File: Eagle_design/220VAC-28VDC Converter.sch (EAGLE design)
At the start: 6 parts, among them J1 1X2-3.5MM, J2 1X2-3.5MM

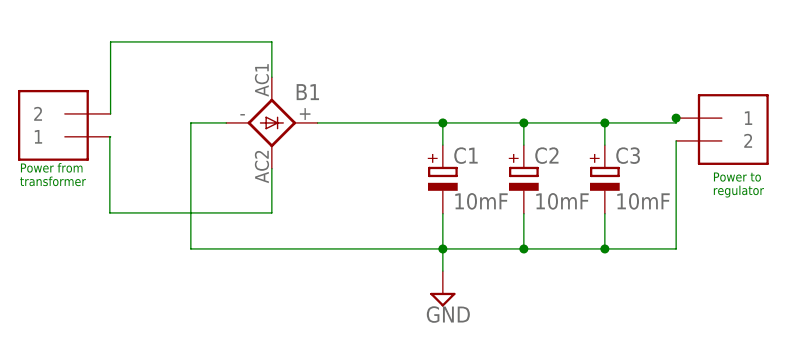
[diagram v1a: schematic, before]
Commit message: Adds labels to the wire connections
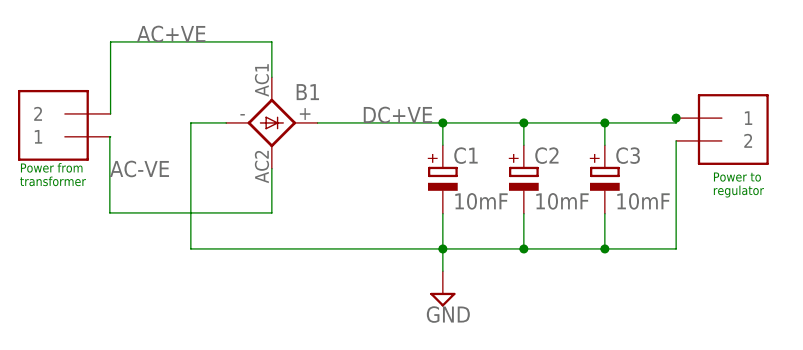
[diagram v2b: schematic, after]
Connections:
- net N$1 renamed AC+VE
- net N$2 renamed AC-VE
- net N$4 renamed DC+VE
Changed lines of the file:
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@@
 <setting verticaltext="up"/>
 </settings>
-<grid distance="0.1" unitdist="inch" unit="inch" style="lines" multiple="1" display="no" altdistance="0.01" altunitdist="inch" altunit="inch"/>
+<grid distance="1" unitdist="mm" unit="mm" style="lines" multiple="1" display="no" altdistance="1" altunitdist="mm" altunit="mm"/>
 <layers>
 <layer number="1" name="Top" color="4" fill="1" visible="no" active="no"/>
@@
 </busses>
 <nets>
-<net name="N$1" class="0">
+<net name="AC+VE" class="0">
 <segment>
 <pinref part="J1" gate="G$1" pin="2"/>
@@
 <pinref part="B1" gate="1" pin="AC1"/>
 <wire x1="45" y1="64.08" x2="45" y2="68" width="0.1524" layer="91"/>
-</segment>
-</net>
-<net name="N$2" class="0">
+<label x="30" y="68" size="1.778" layer="95"/>
+</segment>
+</net>
+<net name="AC-VE" class="0">
 <segment>
 <pinref part="J1" gate="G$1" pin="1"/>
@@
 <pinref part="B1" gate="1" pin="AC2"/>
 <wire x1="45" y1="53.92" x2="45" y2="49" width="0.1524" layer="91"/>
+<label x="27" y="53" size="1.778" layer="95"/>
 </segment>
 </net>
@@
 </segment>
 </net>
-<net name="N$4" class="0">
+<net name="DC+VE" class="0">
 <segment>
 <pinref part="J2" gate="G$1" pin="1"/>
@@
 <wire x1="82" y1="56.54" x2="82" y2="59" width="0.1524" layer="91"/>
 <junction x="82" y="59"/>
-</segment>
-</net>
+<label x="55" y="59" size="1.778" layer="95"/>
+</segment>
+</net>
